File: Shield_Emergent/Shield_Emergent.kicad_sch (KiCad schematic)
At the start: 10 parts

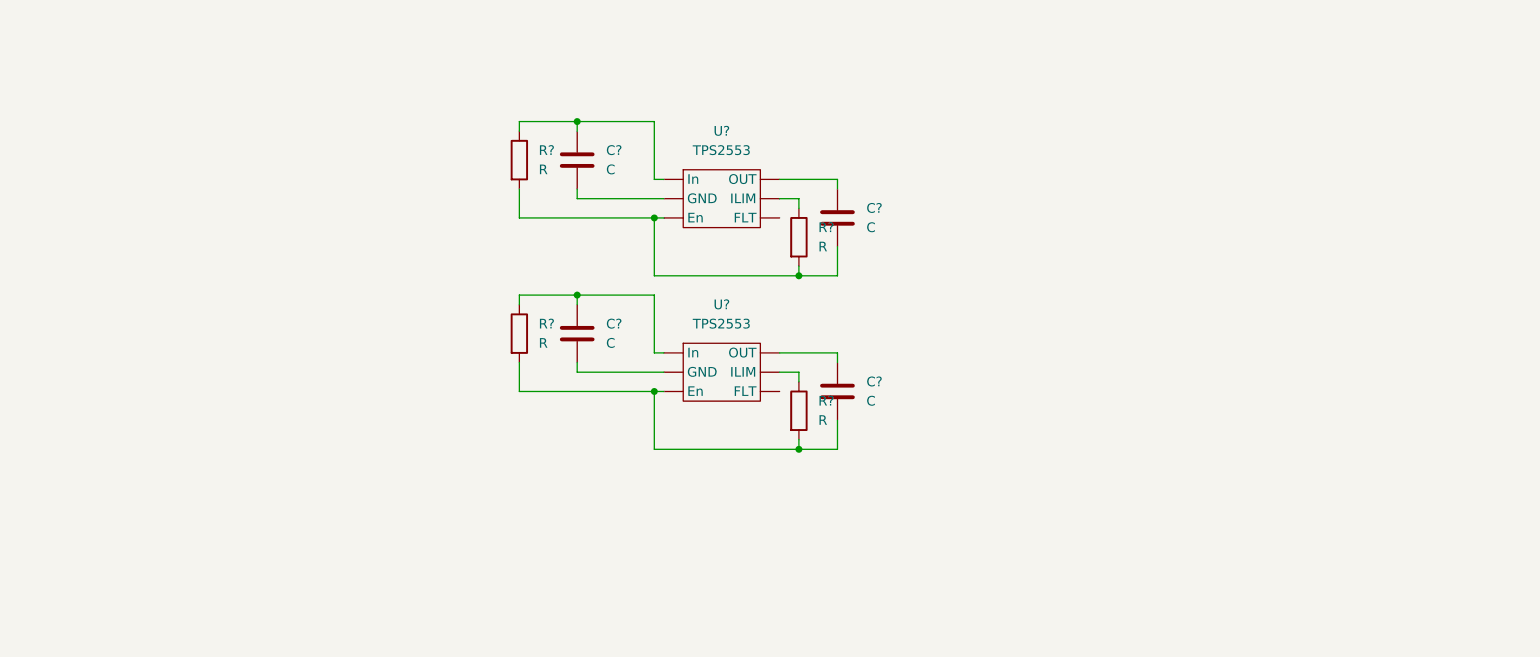
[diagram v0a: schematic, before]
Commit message: v0.2 RPI_Pico symbol&pattern have been added
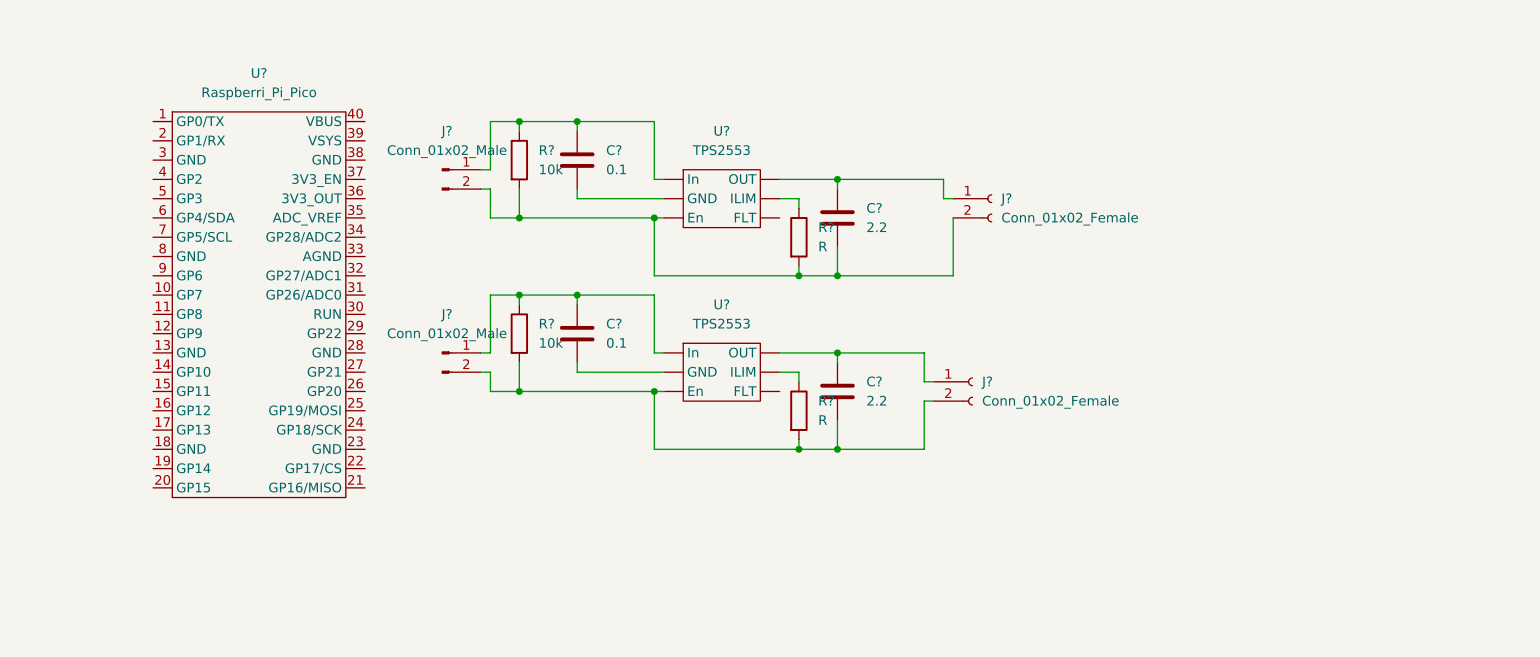
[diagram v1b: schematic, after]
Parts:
- added J? (x2): Conn_01x02_Female, symbol Connector:Conn_01x02_Female
- added J? (x2): Conn_01x02_Male, symbol Connector:Conn_01x02_Male
- added U?: Raspberri_Pi_Pico, symbol Shield_Emergent:Raspberri_Pi_Pico
- C? (x2): value C -> 0.1
- C? (x2): value C -> 2.2
- R? (x2): value R -> 10k
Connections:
- net at C?.2, R?.2, R?.2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: now also J?.2 (Pin_2), J?.2 (Pin_2) (x2)
- net at C?.1, R?.1, U?. (OUT): now also J?.1 (Pin_1) (x2)
- net at U?. (OUT): now also C?.2
- net at C?.1, U?. (OUT): now also J?.1 (Pin_1) (x2)

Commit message: v0.3 Circuit has been corrected
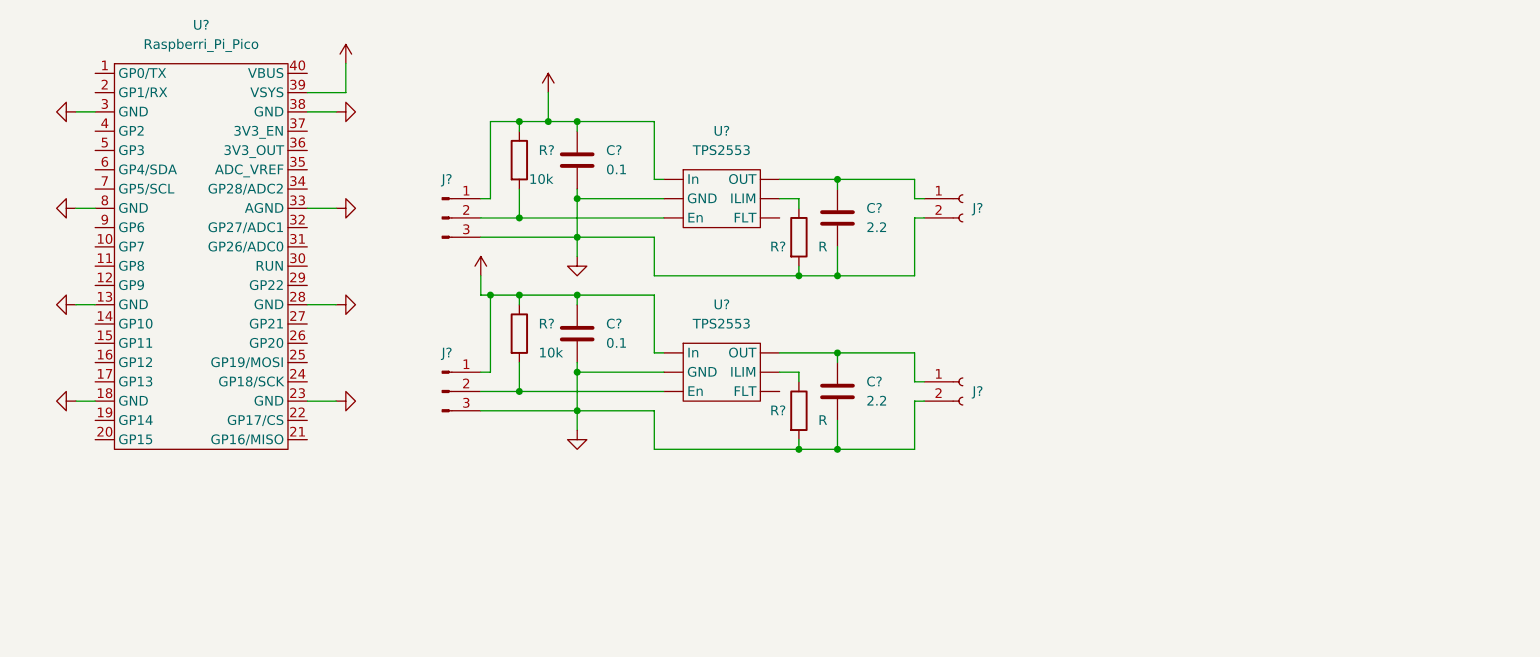
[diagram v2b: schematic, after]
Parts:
- removed J? (x2): Conn_01x02_Male, symbol Connector:Conn_01x02_Male
- added J? (x2): Conn_01x03_Male, symbol Connector:Conn_01x03_Male
- J? (x2): footprint (none) -> Connector_PinSocket_2.54mm:PinSocket_1x02_P2.54mm_Vertical
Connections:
- net GND: now reaches C?.2, J?.2 (Pin_2), R?.2, U?. (OUT)
- net GND: now also C?.2, C?.2, C?.2, J?.2 (Pin_2), R?.2, U?. (OUT), U?.13 (GND), U?.18 (GND), U?.23 (GND), U?.28 (GND), U?.3 (GND), U?.33 (AGND), U?.38 (GND), U?.8 (GND), J?.3 (Pin_3), J?.3 (Pin_3); no longer R?.2
- net VBUS: now reaches C?.1, R?.1, U?. (OUT)
- net VBUS: now also C?.1, R?.1, U?. (OUT), U?.39 (VSYS), J?.1 (Pin_1), J?.1 (Pin_1)
- new net: J?.2 (Pin_2), R?.2, U?. (OUT) (x2)
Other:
- moved on the sheet: J?, U?

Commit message: v0.4 FLT nets have been added
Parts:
- removed J? (x2): Conn_01x03_Male, symbol Connector:Conn_01x03_Male
- added J2, J4: Conn_01x04_Male, Connector_PinSocket_2.54mm:PinSocket_1x04_P2.54mm_Vertical, symbol Connector:Conn_01x04_Male
- added R3, R6: 10k, Resistor_SMD:R_0603_1608Metric_Pad0.98x0.95mm_HandSolder, symbol Device:R
- U1: renamed from U?; footprint (none) -> Shield_Emergent:Raspberry Pi Pico
- U2, U3: renamed from U?; footprint (none) -> Package_TO_SOT_SMD:SOT-23-6_Handsoldering
- gave numbers to parts that had none: 10
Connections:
- net GND: now also J2.3 (Pin_3), J4.3 (Pin_3)
- net VBUS: now also J2.1 (Pin_1), J4.1 (Pin_1), R3.2, R6.2
- net EN1: now reaches R1.2, U2. (OUT)
- net EN1: now also J2.2 (Pin_2)
- net EN2: now reaches R4.2, U3. (OUT)
- net EN2: now also J4.2 (Pin_2)
- new net FLT1: J2.4 (Pin_4), R3.1, U2. (OUT)
- new net FLT2: J4.4 (Pin_4), R6.1, U3. (OUT)
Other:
- moved on the sheet: C1, C2, C3, C4, J1, J3, R1, R2, R4, R5, U2, U3

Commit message: v0.5 Partial decompoition has been completed
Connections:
- net EN1: now also U2.3 (En); no longer U2. (OUT)
- net EN2: now also U3.3 (En); no longer U3. (OUT)
- net FLT1: now also U2.4 (FLT); no longer U2. (OUT)
- net FLT2: now also U3.4 (FLT); no longer U3. (OUT)
- net GND: now also U2.2 (GND), U3.2 (GND); no longer U2. (OUT), U3. (OUT)
- net VBUS: now also U2.1 (In), U3.1 (In); no longer U2. (OUT), U3. (OUT)
- net at R5.1: now also U3.5 (ILIM); no longer U3. (OUT)
- net at C2.1, J1.1 (Pin_1): now also U2.6 (OUT); no longer U2. (OUT)
- net at R2.1: now also U2.5 (ILIM); no longer U2. (OUT)
- net at C4.1, J3.1 (Pin_1): now also U3.6 (OUT); no longer U3. (OUT)
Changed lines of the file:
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@@
     (pin "2")
-  )
-  (symbol (lib_id "Shield_Emergent:TPS2553") (at 175.26 40.64 0) (unit 1)
-    (in_bom yes) (on_board yes) (fields_autoplaced)
-    (property "Reference" "U2" (id 0) (at 175.26 31.75 0))
-    (property "Value" "TPS2553" (id 1) (at 175.26 34.29 0))
-    (property "Footprint" "Package_TO_SOT_SMD:SOT-23-6_Handsoldering" (id 2) (at 175.26 40.64 0)
-      (effects (font (size 1.27 1.27)) hide)
-    )
-    (property "Datasheet" "" (id 3) (at 175.26 40.64 0)
-      (effects (font (size 1.27 1.27)) hide)
-    )
-    (pin "")
-    (pin "")
-    (pin "")
-    (pin "")
-    (pin "")
-    (pin "")
   )
   (symbol (lib_id "Connector:Conn_01x02_Female") (at 219.71 80.01 0) (unit 1)
@@
     (pin "1")
     (pin "2")
-  )
-  (symbol (lib_id "Shield_Emergent:TPS2553") (at 175.26 78.74 0) (unit 1)
-    (in_bom yes) (on_board yes) (fields_autoplaced)
-    (property "Reference" "U3" (id 0) (at 175.26 69.85 0))
-    (property "Value" "TPS2553" (id 1) (at 175.26 72.39 0))
-    (property "Footprint" "Package_TO_SOT_SMD:SOT-23-6_Handsoldering" (id 2) (at 175.26 78.74 0)
-      (effects (font (size 1.27 1.27)) hide)
-    )
-    (property "Datasheet" "" (id 3) (at 175.26 78.74 0)
-      (effects (font (size 1.27 1.27)) hide)
-    )
-    (pin "")
-    (pin "")
-    (pin "")
-    (pin "")
-    (pin "")
-    (pin "")
   )
   (symbol (lib_id "power:VBUS") (at 77.47 25.4 0) (unit 1)
@@
     (pin "2")
   )
+  (symbol (lib_id "Shield_Emergent:TPS2553") (at 175.26 78.74 0) (unit 1)
+    (in_bom yes) (on_board yes) (fields_autoplaced)
+    (property "Reference" "U3" (id 0) (at 175.26 69.85 0))
+    (property "Value" "TPS2553" (id 1) (at 175.26 72.39 0))
+    (property "Footprint" "Package_TO_SOT_SMD:SOT-23-6_Handsoldering" (id 2) (at 175.26 78.74 0)
+      (effects (font (size 1.27 1.27)) hide)
+    )
+    (property "Datasheet" "" (id 3) (at 175.26 78.74 0)
+      (effects (font (size 1.27 1.27)) hide)
+    )
+    (pin "1")
+    (pin "2")
+    (pin "3")
+    (pin "4")
+    (pin "5")
+    (pin "6")
+  )
   (symbol (lib_id "power:GND") (at 76.2 31.75 90) (unit 1)
     (in_bom yes) (on_board yes) (fields_autoplaced)
@@
     (pin "2")
   )
+  (symbol (lib_id "Shield_Emergent:TPS2553") (at 175.26 40.64 0) (unit 1)
+    (in_bom yes) (on_board yes) (fields_autoplaced)
+    (property "Reference" "U2" (id 0) (at 175.26 31.75 0))
+    (property "Value" "TPS2553" (id 1) (at 175.26 34.29 0))
+    (property "Footprint" "Package_TO_SOT_SMD:SOT-23-6_Handsoldering" (id 2) (at 175.26 40.64 0)
+      (effects (font (size 1.27 1.27)) hide)
+    )
+    (property "Datasheet" "" (id 3) (at 175.26 40.64 0)
+      (effects (font (size 1.27 1.27)) hide)
+    )
+    (pin "1")
+    (pin "2")
+    (pin "3")
+    (pin "4")
+    (pin "5")
+    (pin "6")
+  )
   (sheet_instances
     (path "/" (page "1"))
@@
       (reference "U1") (unit 1) (value "Raspberri_Pi_Pico") (footprint "Shield_Emergent:Raspberry Pi Pico")
     )
-    (path "/29d1cdb6-b961-4541-bfed-68be0cb231a5"
+    (path "/fc45f7ed-b122-4152-822e-8c77cda4c79a"
       (reference "U2") (unit 1) (value "TPS2553") (footprint "Package_TO_SOT_SMD:SOT-23-6_Handsoldering")
     )
-    (path "/3aa4fe5b-1850-4c05-acdd-e64a69e4ccb1"
+    (path "/6f19cd9f-5eec-4340-912b-fe7a11209945"
       (reference "U3") (unit 1) (value "TPS2553") (footprint "Package_TO_SOT_SMD:SOT-23-6_Handsoldering")
     )

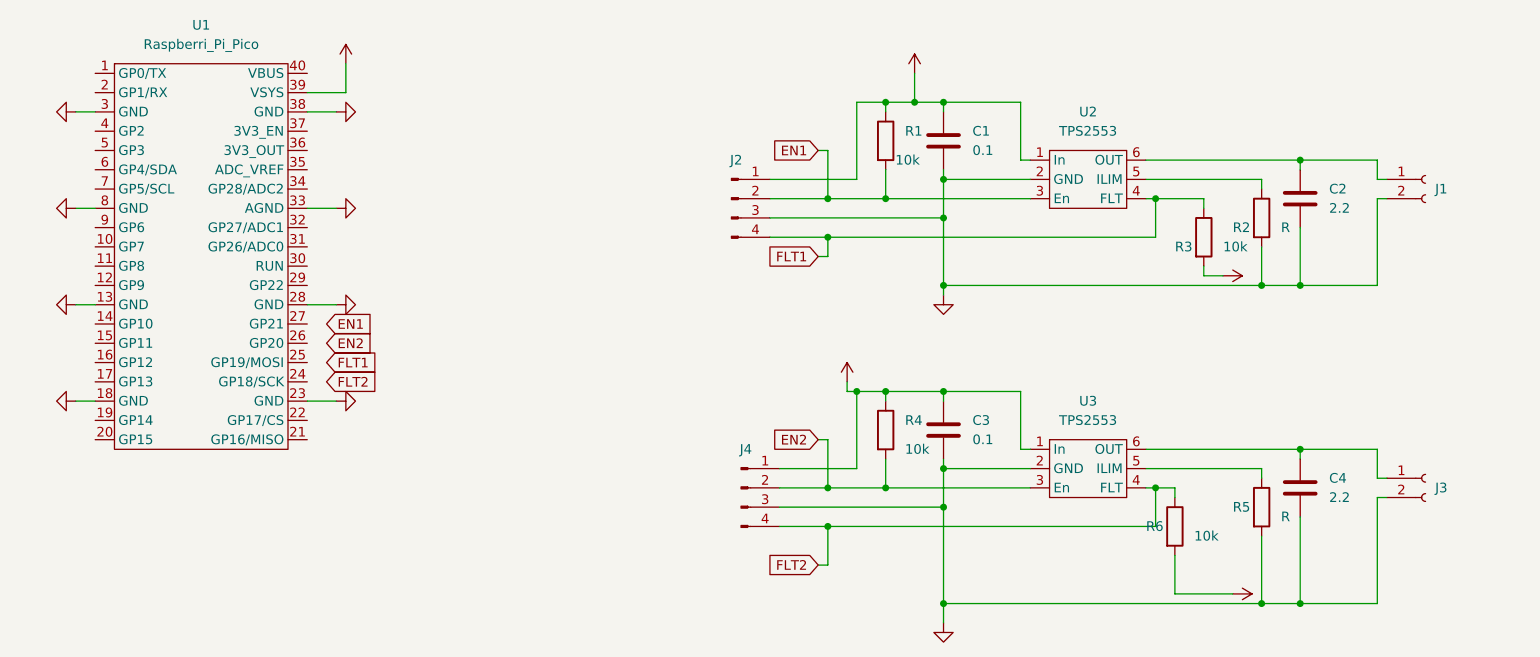
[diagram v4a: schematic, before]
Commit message: v0.6 partially routed
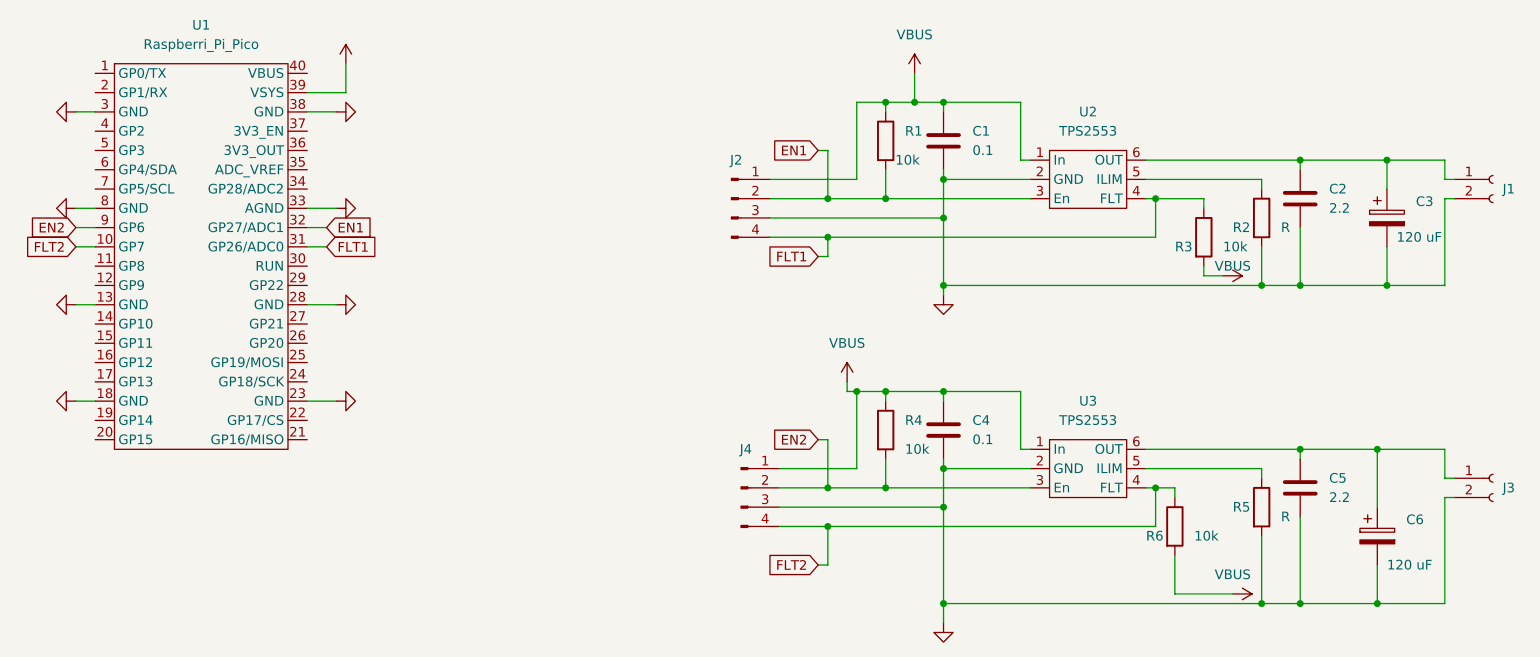
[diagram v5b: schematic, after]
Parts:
- added C3, C6: 120 uF, Capacitor_THT:CP_Radial_D6.3mm_P2.50mm, symbol Device:C_Polarized
- renumbered C3 to C4, C4 to C5
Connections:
- net EN1: now also U1.32 (GP27/ADC1)
- net EN2: now also U1.9 (GP6)
- net FLT1: now also U1.31 (GP26/ADC0)
- net FLT2: now also U1.10 (GP7)
- net GND: now also C3.2, C6.2
- net at C5.1, J3.1 (Pin_1), U3.6 (OUT): now also C6.1
- net at C2.1, J1.1 (Pin_1), U2.6 (OUT): now also C3.1
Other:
- moved on the sheet: J1, J3
